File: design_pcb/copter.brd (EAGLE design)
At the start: 35.6 x 35.6 mm, 54 parts, among them U1 ATMEGA328P-AU, U2 ITG-3200, U3 ADXL345, U4 3.3V, U5 HC_05, U6 IRF9362PBF, U7 IRF9362PBF, U8 HMC5883LSMD, U9 INA169, Y1 8MHZ

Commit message: Add test programs
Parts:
- removed C1: (no value), rcl:C0402
- removed C1_3V3, C1_U4: 4.7uF, SparkFun:0402-CAP
- removed C2: 0.1uF, SparkFun-Passives:0603-CAP
- removed C2_3V3: 0.1uF, SparkFun:0402-CAP
- removed GND_PAD, VIN_PAD: (no value), wirepad:1,6/0,8
- removed R1: (no value), rcl:R0402
- removed R2: 10k, SparkFun-Resistors:0603-RES
- removed R3: (no value), SparkFun-Resistors:AXIAL-0.8
- removed R4: (no value), SparkFun-Resistors:AXIAL-0.4
- removed R5: 10, SparkFun-Resistors:1206
- removed U4: 3.3V, SparkFun:SOT23-5
- added C1_3V1, C1_U9: 4.7uF, SparkFun:0402-CAP
- added C1_U10: 0.1uF, SparkFun-Passives:0603-CAP
- added C2_3V1: 0.1uF, SparkFun:0402-CAP
- added LED1, LED2, LED3, LED4: (no value), led:LED3MM
- added RLOAD: 10k, SparkFun-Resistors:0603-RES
- added RSHUNT_1, RSHUNT_2: (no value), resistor:0309/10
- added RST_C: (no value), rcl:C0402
- added RST_R: (no value), rcl:R0402
- added U10: INA169, SparkFun-AnalogIC:SOT23-5
- added VBAT+, VBAT-: (no value), wirepad:1,6/0,8
- U9: value INA169 -> 3.3V; device SparkFun-AnalogIC:SOT23-5 -> SparkFun:SOT23-5
- moved R7 54.8 mm to (21.6, 24.1), turned to 90 degrees
- moved R6 52.5 mm to (23.2, 24.1), turned to 270 degrees
- moved U9 47.4 mm to (10.4, 33.7), flipped to the bottom, turned to 90 degrees
- moved Y1 13.9 mm to (16.2, 33.4), turned to 270 degrees
- moved C2_U1 11.6 mm to (17.2, 24.1), turned to 270 degrees
- moved C1_U1 11.5 mm to (15.8, 28.5)
- moved C_REF 9.81 mm to (18.7, 24.1), turned to 270 degrees
- moved C2_5V1 7.10 mm to (15.9, 5.08), turned to 270 degrees
- moved R4_PU 6.81 mm to (4.75, 25.3), turned to 180 degrees
- moved C1_U2 6.38 mm to (12.7, 11.1), turned to 270 degrees
- moved C1_U8 5.95 mm to (24.0, 11.7), turned to 180 degrees
- moved R3_PU 5.76 mm to (4.75, 26.8), turned to 180 degrees
- moved J1 5.69 mm to (18.8, 8.10)
- moved U1 5.54 mm to (23.7, 30.4), turned to 270 degrees
- moved C7_U2 5.41 mm to (14.1, 11.1), turned to 90 degrees
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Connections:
- net N$15 renamed MTR4
- net N$31 renamed MTR3
- removed net VOUT: R2.2, R4.P$2, U9.1
- new net I_MEASURE: RLOAD.2, U1.24, U10.1
- new net LED1: LED3.A, U1.12
- new net LED2: LED4.A, U1.16
- new net LED3: LED1.A, U1.11
- new net LED4: LED2.A, U1.2
- net +3V3: now also C1_3V1.1, C2_3V1.1; no longer C1_3V3.1, C2.2, C2_3V3.1, R3.P$1, R5.1, U4.5, U9.3
- net +5V: now also C1_U10.2, RSHUNT_1.1, RSHUNT_2.1, U10.3, U10.5, VBAT+.1; no longer C1_U1.1, C1_U4.1, C2_U1.1, MTR1_2.1, MTR3_2.1, PWR.A, R1.2, RN1.1, RN1.2, U1.18, U1.4, U1.6, U4.1, U4.3, U6.3, U7.3, VIN_PAD.1
- net DTR: now also RST_C.2; no longer C1.2
- net GND: now also C1_3V1.2, C1_U10.1, C1_U9.2, C2_3V1.2, LED1.K, LED2.K, LED3.K, LED4.K, RLOAD.1, U10.2, VBAT-.1; no longer C1_3V3.2, C1_U4.2, C2.1, C2_3V3.2, GND_PAD.1, R2.1, R4.P$1, U4.2
- net RST: now also RST_C.1, RST_R.1; no longer C1.1, R1.1
- net VCC: now also C1_U1.1, C1_U9.1, C2_U1.1, MTR1_2.1, MTR3_2.1, PWR.A, RN1.1, RN1.2, RSHUNT_1.2, RSHUNT_2.2, RST_R.2, U1.18, U1.4, U1.6, U10.4, U6.3, U7.3, U9.1, U9.3; no longer R3.P$2, R5.2, U9.4
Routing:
- net GND: track 175.9 -> 0.00 mm
- net +5V: track 141.8 -> 0.00 mm, vias 1 -> 0
- net +3V3: track 99.6 -> 0.00 mm, vias 6 -> 0
- net RST: track 54.7 -> 0.00 mm, vias 2 -> 0
- net D0/RX: track 52.4 -> 0.00 mm, vias 3 -> 0
- net D1/TX: track 48.5 -> 0.00 mm, vias 3 -> 0
- net SCL: track 37.8 -> 0.00 mm, vias 2 -> 0
- net SDA: track 36.1 -> 0.00 mm, vias 4 -> 0
- net OC2A: track 28.9 -> 0.00 mm, vias 2 -> 0
- net OC1B: track 17.9 -> 0.00 mm
- net OC1A: track 14.2 -> 0.00 mm
- net OC2B: track 14.1 -> 0.00 mm
- net N$14: track 8.15 -> 0.00 mm
- net MTR4: track 7.22 -> 0.00 mm
- net MTR3: track 7.22 -> 0.00 mm
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
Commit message: Update schematic and PCB
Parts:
- removed C1_U10: 0.1uF, SparkFun-Passives:0603-CAP
- removed C1_U9: 4.7uF, SparkFun:0402-CAP
- removed J1: (no value), SparkFun-Connectors:1X05
- removed LED1, LED2, LED3, LED4: (no value), led:LED3MM
- removed R6: 5.1K, resistor:R0402
- removed R7: 1.2K, resistor:R0402
- removed RLOAD: 10k, SparkFun-Resistors:0603-RES
- removed RSHUNT_1, RSHUNT_2: (no value), resistor:0309/10
- removed RST_C: (no value), rcl:C0402
- removed RST_R: (no value), rcl:R0402
- removed VBAT+, VBAT-: (no value), wirepad:1,6/0,8
- added C1: (no value), rcl:C0402
- added C1_U5: 4.7uF, SparkFun:0402-CAP
- added C_IMEASURE: 0.1uF, SparkFun-Passives:0603-CAP
- added GND_PAD, VIN_PAD: (no value), wirepad:1,6/0,8
- added R1: (no value), rcl:R0402
- added R1_DIV: 5.1K, resistor:R0402
- added R2_DIV: 1.2K, resistor:R0402
- added R_LOAD: (no value), resistor:0309/10
- added R_SHUNT: 10k, SparkFun-Resistors:0603-RES
- added X1: 05-JST-B5B-XH-A, bt_con-jst-xh:B5B-XH
- moved C2_5V1 29.6 mm to (10.8, 34.3), turned to 0 degrees
- moved C1_5V1 22.6 mm to (9.63, 30.6), turned to 270 degrees
- moved Y1 13.9 mm to (26.0, 23.5), turned to 90 degrees
- moved PWR3V 12.1 mm to (8.89, 1.91)
- moved C2_U1 11.6 mm to (24.1, 33.4), turned to 90 degrees
- moved C1_U1 11.5 mm to (26.7, 32.4)
- moved PWR 11.4 mm to (10.8, 1.91)
- moved RN1 11.4 mm to (11.4, 5.08)
- moved TX 10.8 mm to (12.8, 1.91)
- moved RX 10.2 mm to (14.6, 1.91)
- moved U9 9.86 mm to (5.08, 25.4), turned to 0 degrees
- moved C_REF 9.18 mm to (19.1, 33.3), turned to 180 degrees
- moved R4_PU 6.81 mm to (11.5, 24.4), turned to 270 degrees
- moved C1_U2 6.38 mm to (6.99, 14.0), turned to 180 degrees
- moved C1_U8 5.95 mm to (21.6, 17.1), turned to 270 degrees
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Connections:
- net MTR3 renamed N$31
- net MTR4 renamed N$15
- removed net LED1: LED3.A, U1.12
- removed net LED2: LED4.A, U1.16
- removed net LED3: LED1.A, U1.11
- removed net LED4: LED2.A, U1.2
- net +3V3: now also C_IMEASURE.2, U10.5
- net +5V: now also C1_U1.1, C1_U5.1, C2_U1.1, PWR.A, R1.2, R1_DIV.2, RN1.1, RN1.2, R_LOAD.1, U1.18, U1.4, U1.6, U9.1, U9.3, VIN_PAD.1, X1.P$5; no longer C1_U10.2, J1.5, R6.2, RSHUNT_1.1, RSHUNT_2.1, U10.5, VBAT+.1
- net D0/RX: now also X1.P$2; no longer J1.2
- net D1/TX: now also X1.P$3; no longer J1.3
- net DTR: now also C1.2, X1.P$4; no longer J1.4, RST_C.2
- net GND: now also C1_U5.2, C_IMEASURE.1, GND_PAD.1, R2_DIV.1, R_SHUNT.1, X1.P$1; no longer C1_U10.1, C1_U9.2, J1.1, LED1.K, LED2.K, LED3.K, LED4.K, R7.1, RLOAD.1, VBAT-.1
- net I_MEASURE: now also R_SHUNT.2; no longer RLOAD.2
- net RST: now also C1.1, R1.1; no longer RST_C.1, RST_R.1
- net VCC: now also R_LOAD.2; no longer C1_U1.1, C1_U9.1, C2_U1.1, PWR.A, RN1.1, RN1.2, RSHUNT_1.2, RSHUNT_2.2, RST_R.2, U1.18, U1.4, U1.6, U9.1, U9.3
- net V_MEASURE: now also R1_DIV.1, R2_DIV.2; no longer R6.1, R7.2

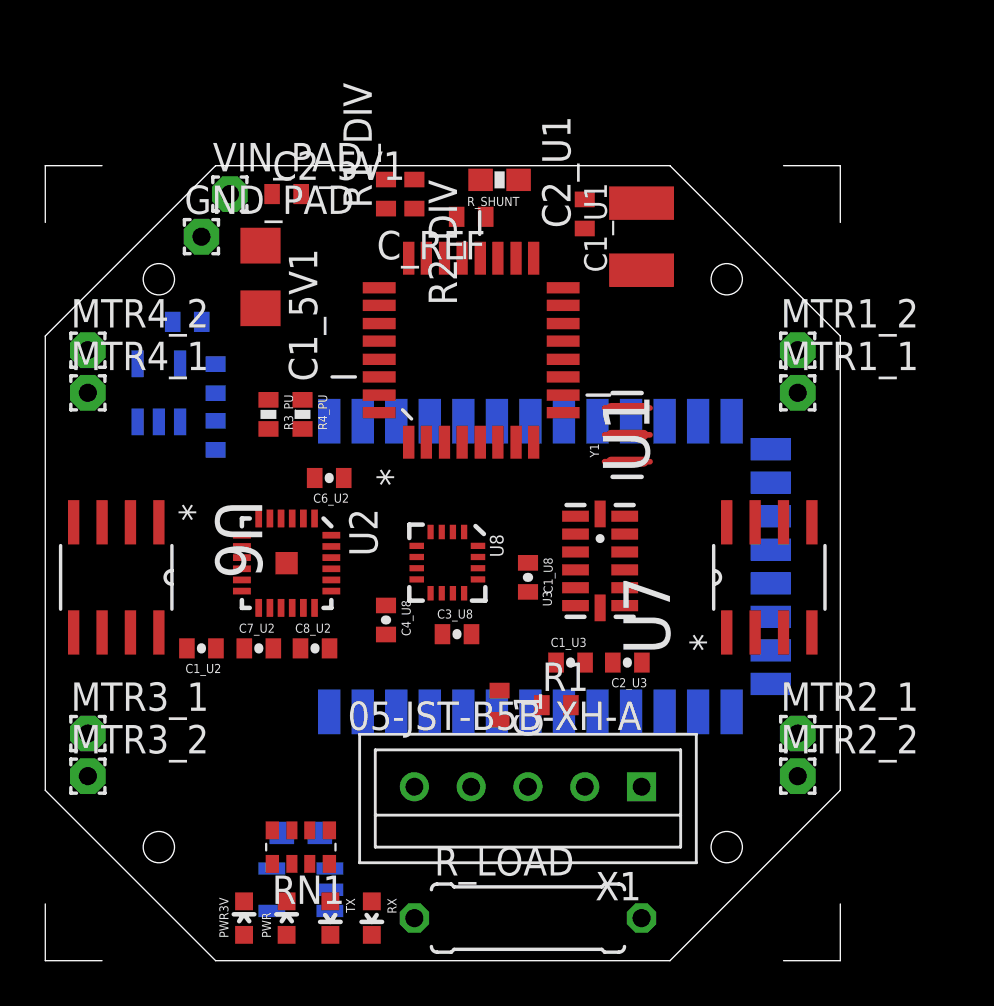
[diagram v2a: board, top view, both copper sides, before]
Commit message: move some components
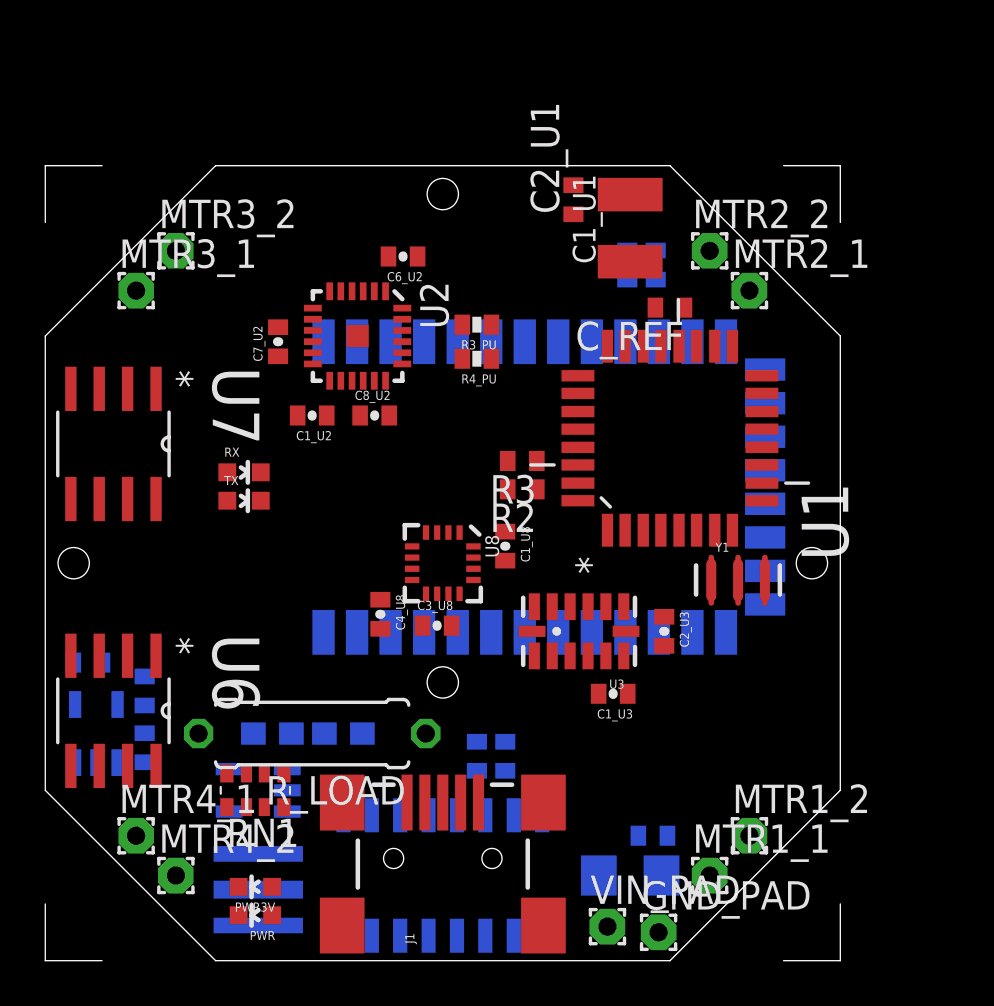
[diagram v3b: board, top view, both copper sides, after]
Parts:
- removed X1: 05-JST-B5B-XH-A, bt_con-jst-xh:B5B-XH
- added J1: USB-MINIB-5PIN, SparkFun-Connectors:USB-MINIB
- added R2, R3: 1k, resistor:R0402
- added U$1: CH340G, usb-serial:SOIC16
- added U$2: CSTCV, murata-cstcc-cstce-cstcr-cstcv-resonators:CSTCV
- moved GND_PAD 37.2 mm to (27.4, 1.27)
- moved VIN_PAD 36.9 mm to (25.1, 1.52)
- moved C2_5V1 33.0 mm to (27.2, 5.59), flipped to the bottom, turned to 180 degrees
- moved C1_5V1 31.5 mm to (26.2, 3.81), flipped to the bottom, turned to 180 degrees
- moved U7 29.9 mm to (3.05, 23.1), turned to 270 degrees
- moved R_SHUNT 25.7 mm to (13.3, 10.2), flipped to the bottom
- moved MTR4_2 23.8 mm to (5.84, 3.81)
- moved MTR2_2 23.8 mm to (29.7, 31.8)
- moved MTR3_2 23.8 mm to (5.84, 31.8)
- moved MTR1_1 21.9 mm to (29.7, 3.81)
- moved MTR1_2 21.8 mm to (31.5, 5.59)
- moved RX 20.7 mm to (8.89, 21.8), turned to 270 degrees
- moved MTR2_1 19.9 mm to (31.5, 30.0)
- moved MTR3_1 19.9 mm to (4.06, 30.0)
- moved MTR4_1 19.9 mm to (4.06, 5.59)
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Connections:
- new net D+: J1.D+, U$1.5
- new net D-: J1.D-, U$1.6
- new net N$1: R2.2, U$1.2
- new net N$16: U$1.7, U$2.IN
- new net N$4: R3.2, U$1.3
- new net N$9: U$1.8, U$2.OUT
- new net SPI_RX: R3.1, U1.30
- new net SPI_TX: R2.1, U1.31
- net +5V: now also J1.VBUS, U$1.16; no longer X1.P$5
- net D0/RX: now also U1.32; no longer U1.30, X1.P$2
- net D1/TX: now also U1.2; no longer U1.31, X1.P$3
- net DTR: now also U$1.13; no longer X1.P$4
- net GND: now also J1.GND, U$1.1, U$2.GND; no longer X1.P$1

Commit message: replace *4 resistor with 4 separate resistors
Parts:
- removed C1_5V1: 4.7uF, resistor:C1206
- removed C2_5V1: 0.01uF, resistor:C0402
- removed RN1: (no value), resistor-dil:EXB38V
- added C1_5V: 4.7uF, rcl:C1210K
- added C2_5V: 0.01uF, resistor:C0402
- added R4, R5, R6, R7: 4.7k, rcl:R0402
- C1_U1: device rcl:C1210K -> resistor:C1206
- moved MTR1_1 36.8 mm to (5.84, 31.8)
- moved MTR2_2 36.8 mm to (5.84, 3.81)
- moved MTR1_2 36.7 mm to (4.06, 30.0)
- moved MTR2_1 36.7 mm to (4.06, 5.59)
- moved U6 29.7 mm to (32.8, 11.4)
- moved C1_3V1 28.5 mm to (30.2, 9.91), turned to 180 degrees
- moved MTR3_1 27.4 mm to (31.5, 30.0)
- moved MTR4_1 27.4 mm to (31.5, 5.59)
- moved C2_3V1 26.1 mm to (30.2, 8.13), turned to 180 degrees
- moved U9 25.2 mm to (27.4, 9.14)
- moved MTR3_2 23.9 mm to (29.7, 31.8)
- moved MTR4_2 23.9 mm to (29.7, 3.81)
- moved C1_U5 20.8 mm to (25.1, 7.37), turned to 270 degrees
- moved R2_DIV 20.0 mm to (22.6, 11.7), turned to 90 degrees
- moved R1_DIV 19.6 mm to (23.9, 11.7), turned to 270 degrees
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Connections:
- net AREF renamed N$17
- net +5V: now also C1_5V.1, C2_5V.1; no longer C1_5V1.1, C1_U1.1, C2_5V1.1, C2_U1.1, R1.2, RN1.1, RN1.2, U$1.16, U1.18, U1.4, U1.6
- net GND: now also C1_5V.2, C2_5V.2, R4.1, R5.1; no longer C1_5V1.2, C2_5V1.2, RN1.3, RN1.4
- net N$3: now also R7.2; no longer RN1.7
- net N$5: now also R6.2; no longer RN1.8
- net N$6: now also R4.2; no longer RN1.6
- net N$8: now also R5.2; no longer RN1.5
- net VCC: now also C1_U1.1, C2_U1.1, R1.2, R6.1, R7.1, U$1.16, U1.18, U1.4, U1.6

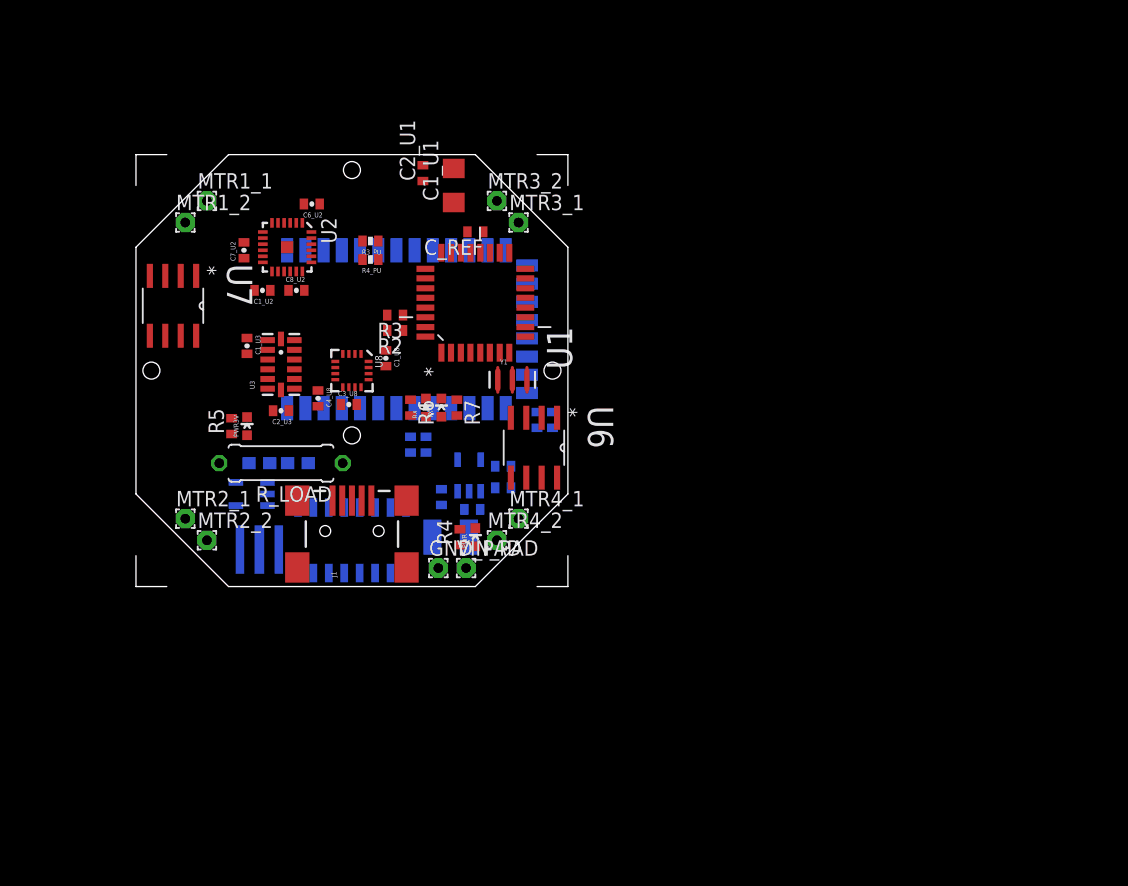
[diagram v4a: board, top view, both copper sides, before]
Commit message: add breakout boards
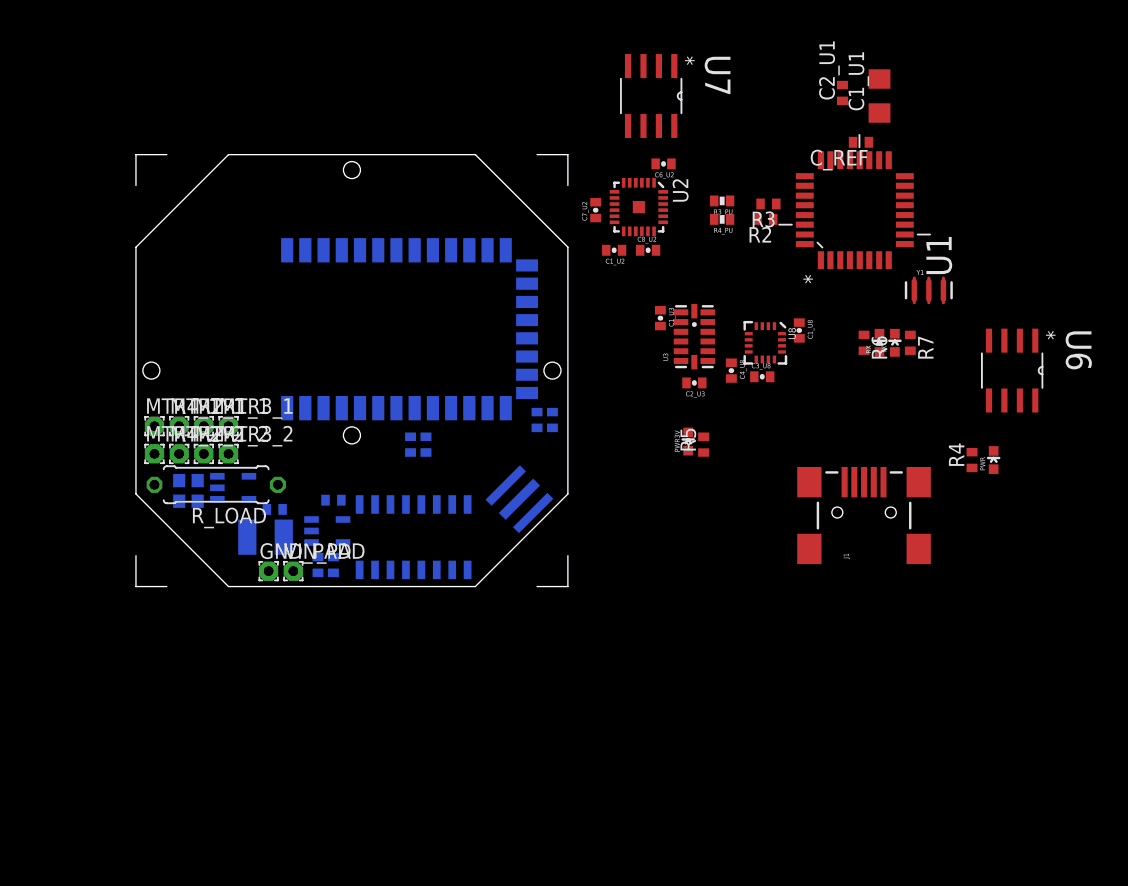
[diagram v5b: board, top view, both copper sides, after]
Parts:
- removed C1_U5: 4.7uF, SparkFun:0402-CAP
- added C1_U9: 4.7uF, SparkFun:0402-CAP
- moved PWR 43.1 mm to (70.6, 10.4)
- moved U7 43.0 mm to (42.4, 40.4)
- moved R4 42.6 mm to (68.8, 10.4)
- moved J1 42.2 mm to (59.9, 6.10)
- moved U6 39.9 mm to (72.1, 17.8)
- moved R5 38.9 mm to (46.7, 11.7)
- moved R6 37.7 mm to (59.9, 20.1)
- moved TX 37.7 mm to (62.5, 20.1)
- moved R7 37.7 mm to (63.8, 20.1)
- moved RX 37.7 mm to (61.2, 20.1)
- moved PWR3V 36.3 mm to (45.5, 11.9)
- moved C1_U1 35.8 mm to (61.2, 40.4)
- moved C2_U1 35.2 mm to (58.2, 40.6)
- moved Y1 35.1 mm to (65.3, 24.4)
- moved C1_U3 34.1 mm to (43.2, 22.1)
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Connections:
- net +3V3: now also R1.2, U1.18, U1.4, U1.6; no longer C_IMEASURE.2, U10.5
- net +5V: now also C_IMEASURE.2, U10.5; no longer C1_U5.1, U9.1, U9.3
- net GND: now also C1_U9.2; no longer C1_U5.2
- net VCC: now also C1_U9.1, U9.1, U9.3; no longer R1.2, U1.18, U1.4, U1.6
